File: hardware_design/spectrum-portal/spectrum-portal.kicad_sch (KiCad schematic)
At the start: 18 parts, among them J1 PJ398SM, J2 PJ398SM, J3 J998-ND, J4 PJ398SM, J5 PJ398SM, J6 J998-ND, J7 SBH11-PBPC-D05-ST-BK, U1 TL072IDR

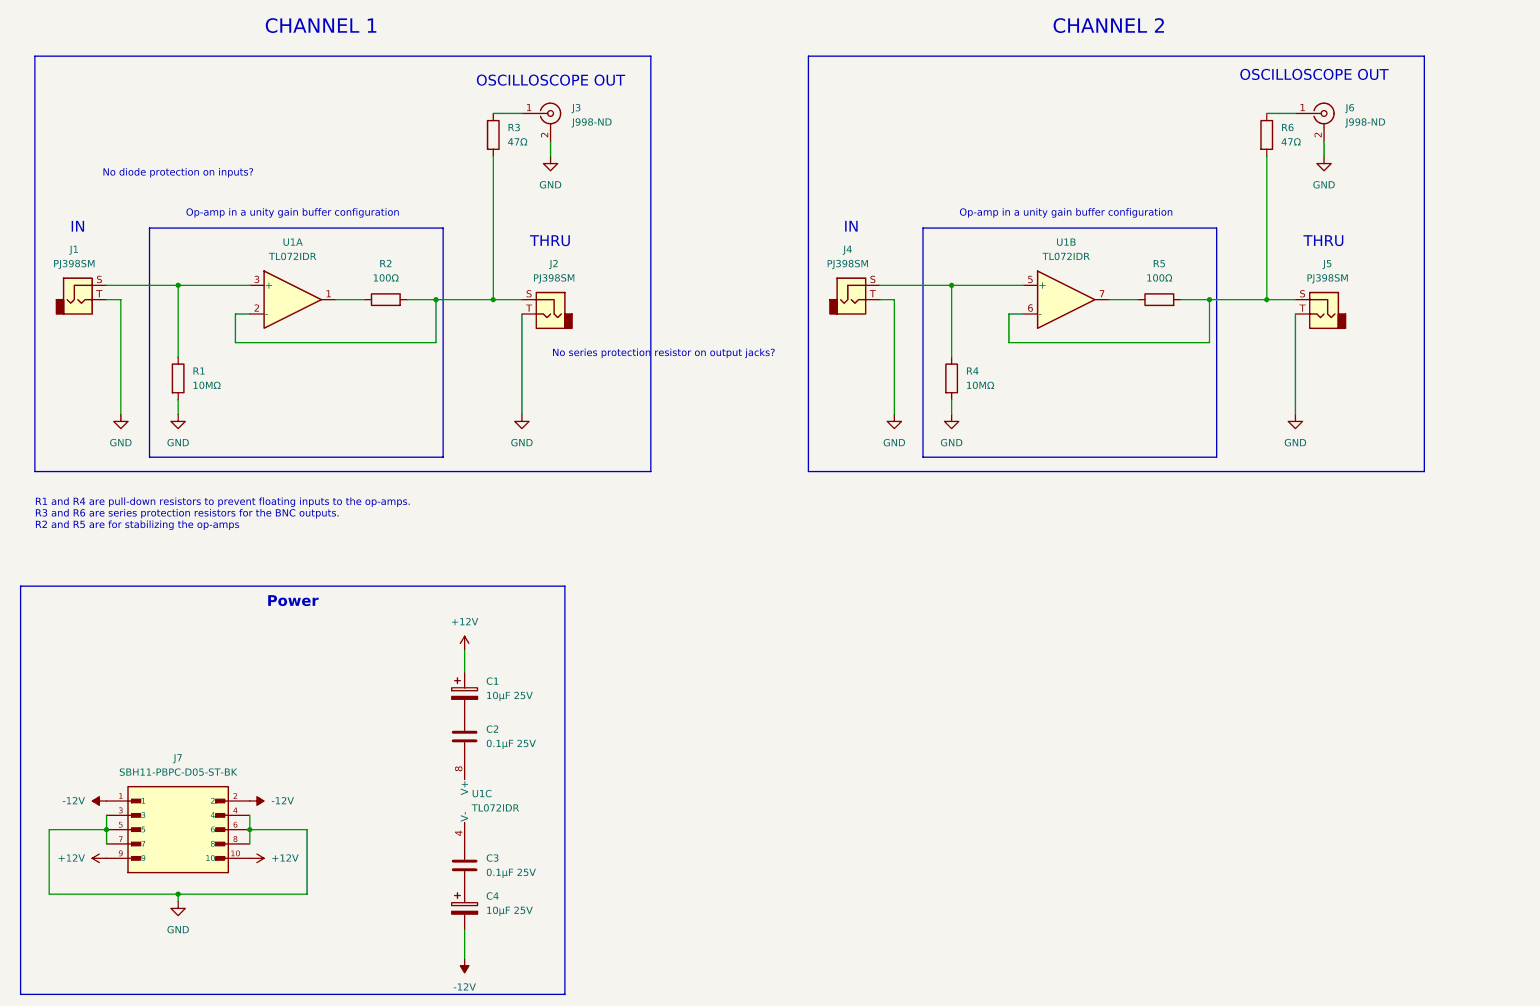
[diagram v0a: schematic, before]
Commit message: Redesigned as 5HP, added protection components
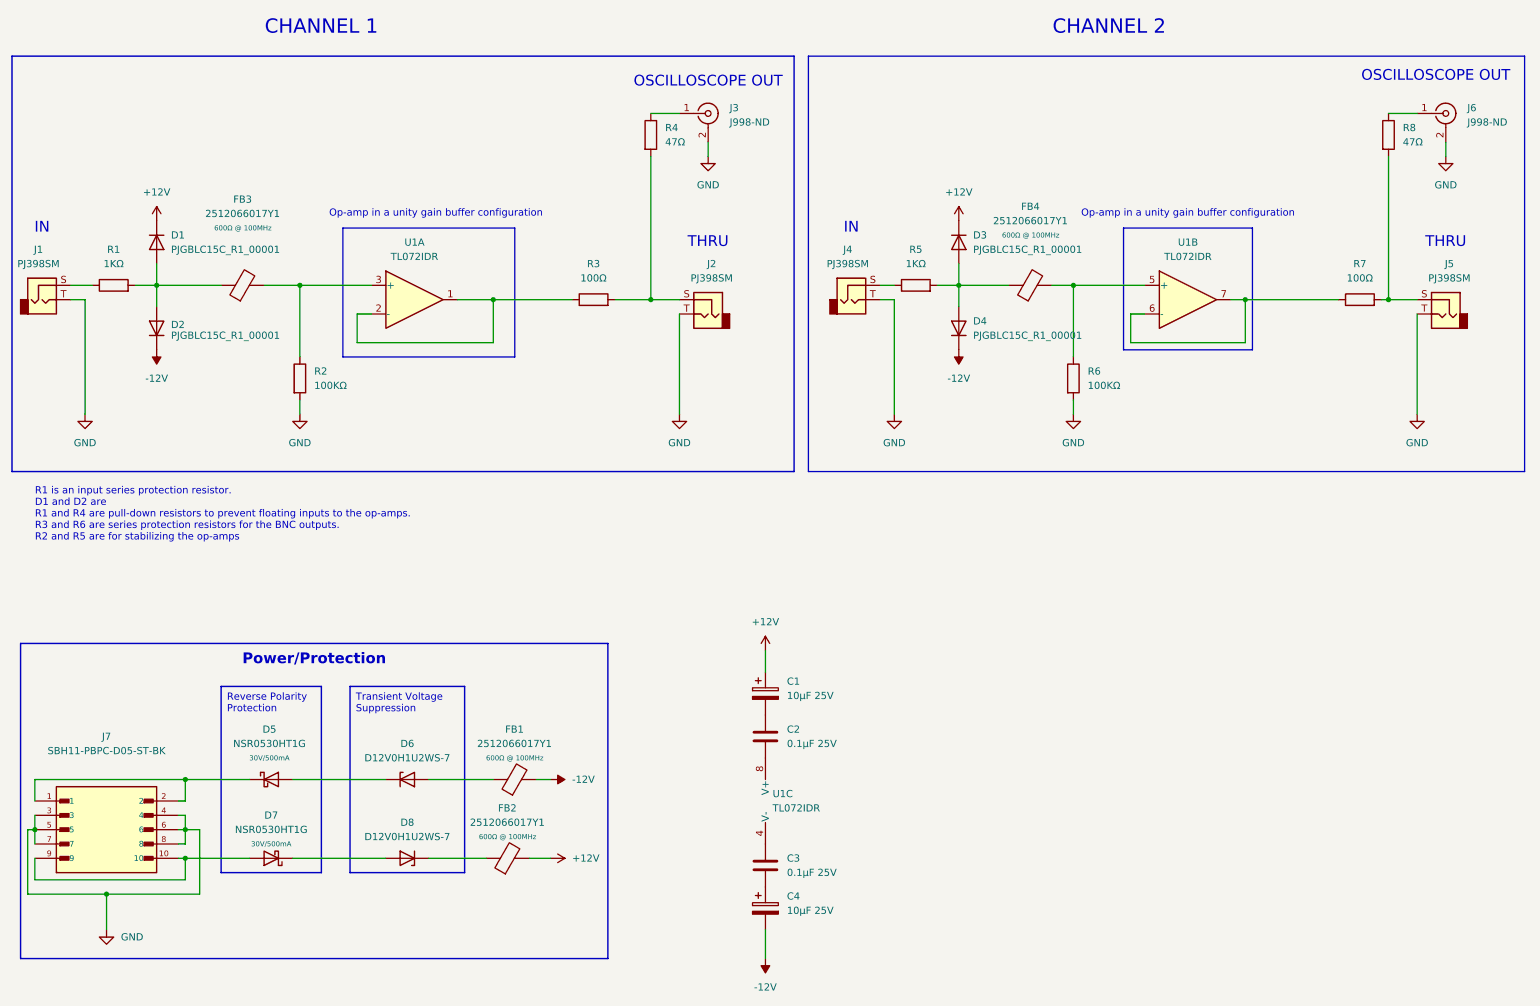
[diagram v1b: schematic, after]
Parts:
- added D1, D2, D3, D4: PJGBLC15C_R1_00001, Diode_SMD:D_SOD-323_HandSoldering, symbol Device:D
- added D5, D7: NSR0530HT1G, Diode_SMD:D_SOD-323_HandSoldering, symbol Device:D_Schottky
- added D6, D8: D12V0H1U2WS-7, Diode_SMD:D_SOD-323_HandSoldering, symbol Device:D_Zener
- added FB1, FB2, FB3, FB4: 2512066017Y1, Inductor_SMD:L_1206_3216Metric_Pad1.42x1.75mm_HandSolder, symbol Device:FerriteBead
- added R1, R5: 1KΩ, Resistor_SMD:R_1206_3216Metric_Pad1.30x1.75mm_HandSolder, symbol Device:R
- R2: renamed from R1; value 10MΩ -> 100KΩ
- R6: renamed from R4; value 10MΩ -> 100KΩ
- renumbered R2 to R3, R3 to R4, R5 to R7, R6 to R8
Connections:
- net +12V: now also D1.1 (K), D3.1 (K), FB2.2; no longer J7.10, J7.9
- net -12V: now also D2.1 (K), D4.1 (K), FB1.2; no longer J7.1, J7.2
- net at R6.1, U1.5 (+): now also FB4.2; no longer J4.S
- net at J5.S, R7.2, R8.2: no longer U1.6 (-)
- net at R7.1, U1.7: now also U1.6 (-)
- net at J2.S, R3.2, R4.2: no longer U1.2 (-)
- net at R2.1, U1.3 (+): now also FB3.2; no longer J1.S
- net at R3.1, U1.1: now also U1.2 (-)
- new net: D3.2 (A), D4.2 (A), FB4.1, R5.2
- new net: D1.2 (A), D2.2 (A), FB3.1, R1.2
- new net: D8.1 (K), FB2.1
- new net: J1.S, R1.1
- new net: J4.S, R5.1
- new net: D5.1 (K), J7.1, J7.2
- new net: D5.2 (A), D6.1 (K)
- new net: D6.2 (A), FB1.1
- new net: D7.1 (K), D8.2 (A)
- new net: D7.2 (A), J7.10, J7.9
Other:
- note added: "R1 is an input series protection resistor. D1 and D2 are R1 and R4 are pull-down resistors to prevent floating inputs to the op-amps. R3 and R6 are series protection resistors for the BNC outputs. R2 and R5 are for stabilizing the op-amps"
- note removed: "No diode protection on inputs?"
- note removed: "No series protection resistor on output jacks?"
- note removed: "R1 and R4 are pull-down resistors to prevent floating inputs to the op-amps. R3 and R6 are series protection resistors for the BNC outputs. R2 and R5 are for stabilizing the op-amps"
- moved on the sheet: C1, C2, C3, C4, J1, J2, J3, J5, J6, J7, R2, R3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

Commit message: Switch to more affordable SMA connector
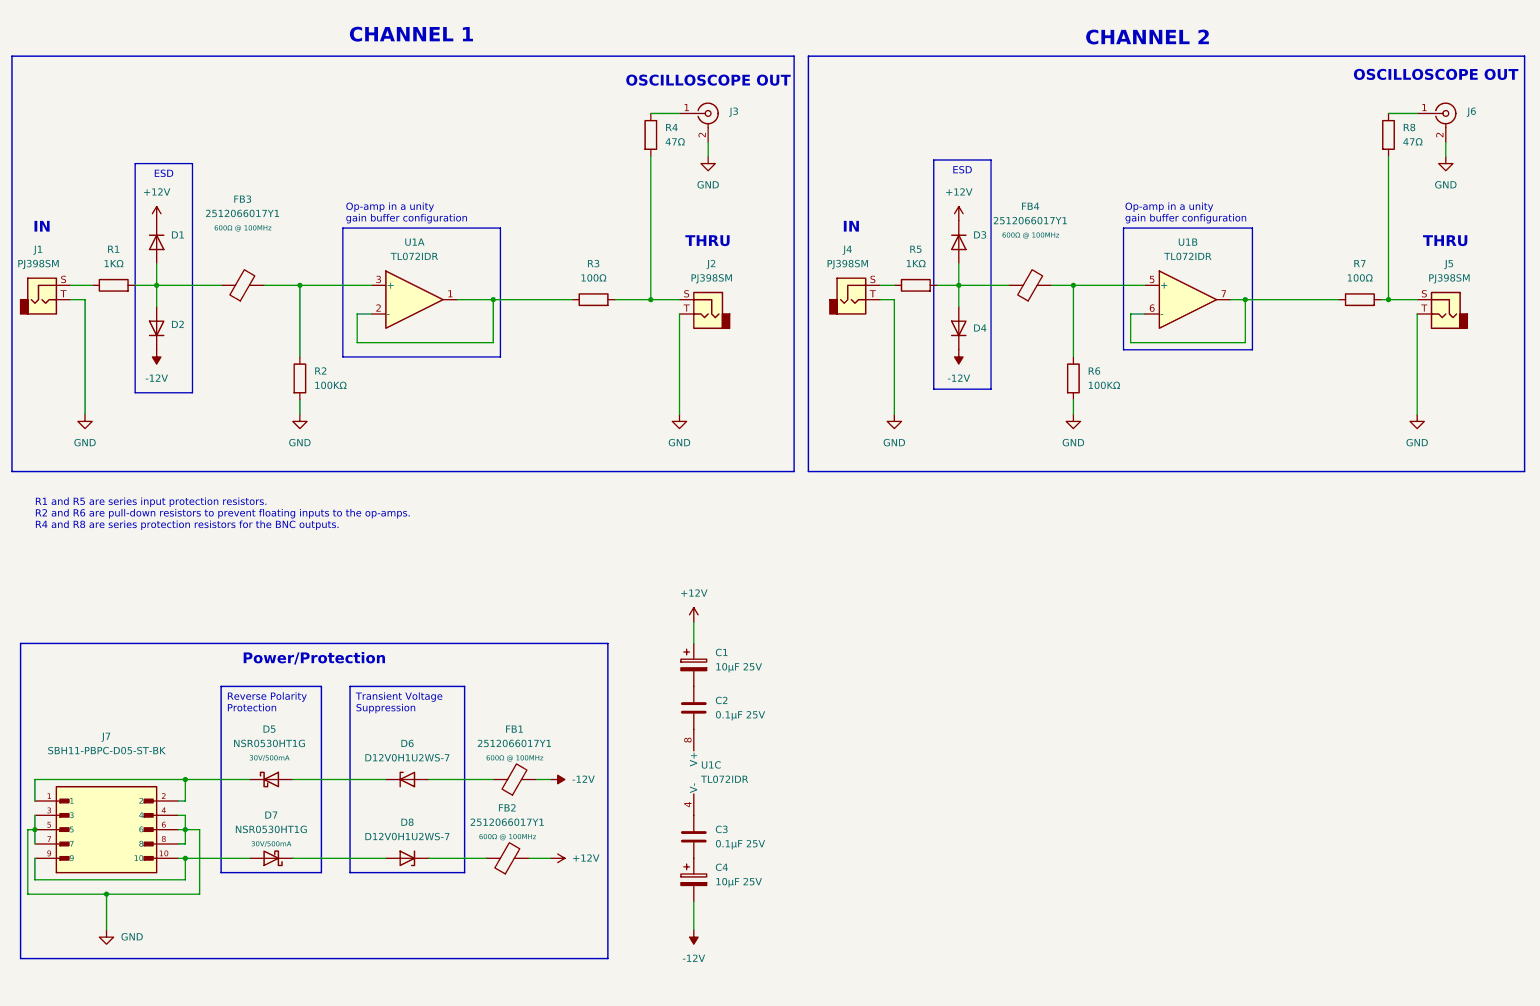
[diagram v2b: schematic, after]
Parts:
- C1, C4: URL https://www.digikey.ca/short/j2zw22p9 -> (none)
- C2, C3: DIGIKEY_PART 399-9776-ND -> 4713-GMT31X5R106K50NT2CT-ND; MANUFACTURER Kemet -> (none)
- D7: DIGIKEY_PART (none) -> NSR0530HT1GOSCT-ND
- FB1, FB2, FB3, FB4: DIGIKEY_PART (none) -> 1934-1489-1-ND
- J1, J2, J4, J5: DIGIKEY_PART (none) -> NOT DIGIKEY PRODUCT
- J3, J6: value J998-ND -> ~; footprint SMA:LINX_CONSMA008-G -> SMA:CONN_132291_AMP; DIGIKEY_PART J998-ND -> ACX1976-ND; MANUFACTURER Cinch Connectivity Solutions Johnson -> (none)
- J7: MANUFACTURER Sullins Connector Solutions -> (none); MAXIMUM_PACKAGE_HEIGHT 9.1mm -> (none); PARTREV J -> (none); SNAPEDA_PN SBH11-PBPC-D05-ST-BK -> (none); STANDARD Manufacturer Recommendations -> (none)
- R1, R5: DIGIKEY_PART (none) -> 311-1.00KFRCT-ND
- R2, R6: DIGIKEY_PART RNF14FTD10M0CT-ND -> 311-100KFRCT-ND
- R3, R7: DIGIKEY_PART RNF14FTD100RCT-ND -> 311-100FRCT-ND
- R4: DIGIKEY_PART S47CATR-ND -> 311-47.0FRCT-ND; Rating (none) -> 1% 1/4W
- R8: DIGIKEY_PART S47CATR-ND -> 311-47.0FRCT-ND
- U1: MANUFACTURER Texas Instruments -> (none)
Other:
- note added: "R1 and R5 are series input protection resistors. R2 and R6 are pull-down resistors to prevent floating inputs to the op-amps. R4 and R8 are series protection resistors for the BNC outputs."
- note removed: "R1 is an input series protection resistor. D1 and D2 are R1 and R4 are pull-down resistors to prevent floating inputs to the op-amps. R3 and R6 are series protection resistors for the BNC outputs. R2 and R5 are for stabilizing the op-amps"
- moved on the sheet: C1, C2, C3, C4, U1C

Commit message: Redesigned as passive module in 3HP
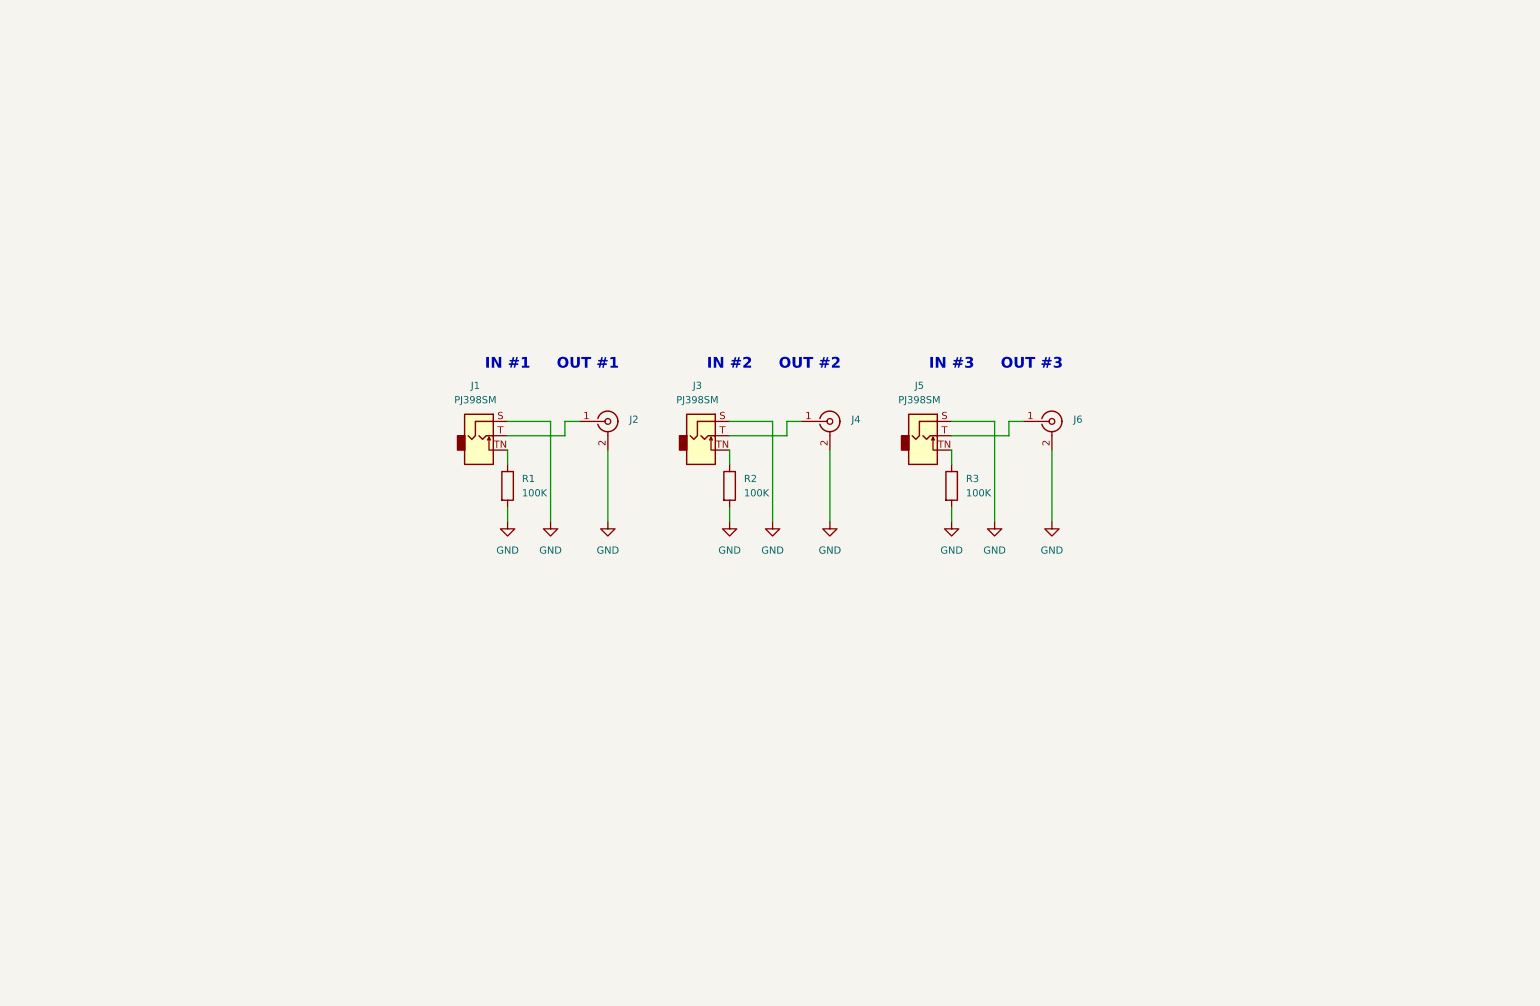
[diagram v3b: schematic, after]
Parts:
- removed C1, C4: 10µF 25V, Capacitor_THT:CP_Radial_D4.0mm_P1.50mm, symbol Device:C_Polarized
- removed C2, C3: 0.1µF 25V, Capacitor_SMD:C_1206_3216Metric_Pad1.33x1.80mm_HandSolder, symbol Device:C
- removed D1, D2, D3, D4: PJGBLC15C_R1_00001, Diode_SMD:D_SOD-323_HandSoldering, symbol Device:D
- removed D5, D7: NSR0530HT1G, Diode_SMD:D_SOD-323_HandSoldering, symbol Device:D_Schottky
- removed D6, D8: D12V0H1U2WS-7, Diode_SMD:D_SOD-323_HandSoldering, symbol Device:D_Zener
- removed FB1, FB2, FB3, FB4: 2512066017Y1, Inductor_SMD:L_1206_3216Metric_Pad1.42x1.75mm_HandSolder, symbol Device:FerriteBead
- removed J1, J2, J4, J5: PJ398SM, Thonk:Jack_3.5mm_QingPu_WQP-PJ398SM_Vertical, symbol Connector_Audio:AudioJack2
- removed J7: SBH11-PBPC-D05-ST-BK, EurorackPowerConnector:SULLINS_SBH11-PBPC-D05-ST-BK, symbol Eurorack_Power_Connector:SBH11-PBPC-D05-ST-BK
- removed R4, R8: 47Ω, Resistor_SMD:R_1206_3216Metric_Pad1.30x1.75mm_HandSolder, symbol Device:R
- removed R5: 1KΩ, Resistor_SMD:R_1206_3216Metric_Pad1.30x1.75mm_HandSolder, symbol Device:R
- removed R6: 100KΩ, Resistor_SMD:R_1206_3216Metric_Pad1.30x1.75mm_HandSolder, symbol Device:R
- removed R7: 100Ω, Resistor_SMD:R_1206_3216Metric_Pad1.30x1.75mm_HandSolder, symbol Device:R
- removed U1: TL072IDR, TL072:SOIC127P599X175-8N, symbol Amplifier_Operational:TL072
- added J1, J3, J5: PJ398SM, Thonk:Jack_3.5mm_QingPu_WQP-PJ398SM_Vertical, symbol Connector_Audio:AudioJack2_SwitchT
- added J4: ~, SMA:CONN_132291_AMP, symbol Connector:Conn_Coaxial
- R1: value 1KΩ -> 100K; DIGIKEY_PART 311-1.00KFRCT-ND -> (none)
- R2: value 100KΩ -> 100K; DIGIKEY_PART 311-100KFRCT-ND -> (none)
- R3: value 100Ω -> 100K; DIGIKEY_PART 311-100FRCT-ND -> (none)
- renumbered J3 to J2
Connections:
- net GND: now also R1.2, R3.2, J1.S, J3.S, J4.2 (Ext), J5.S
- net at J2.1 (In): now also J1.T
- net at R2.1: now also J3.TN
- net at J6.1 (In): now also J5.T
- net at R1.1: now also J1.TN
- net at R3.1: now also J5.TN
- new net: J3.T, J4.1 (In)
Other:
- note added: "IN #1"
- note added: "IN #2"
- note added: "IN #3"
- note added: "OUT #1"
- note added: "OUT #2"
- note added: "OUT #3"
- note removed: "CHANNEL 1"
- note removed: "CHANNEL 2"
- note removed: "IN"
- note removed: "OSCILLOSCOPE OUT"
- note removed: "Op-amp in a unity gain buffer configuration"
- note removed: "R1 and R5 are series input protection resistors. R2 and R6 are pull-down resistors to prevent floating inputs to the op-amps. R4 and R8 are series protection resistors for the BNC outputs."
- note removed: "THRU"
- moved on the sheet: J2
